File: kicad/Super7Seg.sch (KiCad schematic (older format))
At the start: 37 parts, among them CON1 AVR-ISP-6, IC1 ATMEGA328P-P, IC2 74HC238, P1 CONN_01X13, P2 CONN_01X09, P3 CONN_01X13, P4 CONN_01X09, P5 UART, P6 CONN_01X02, P7 CONN_01X02, U1 ULN2003A

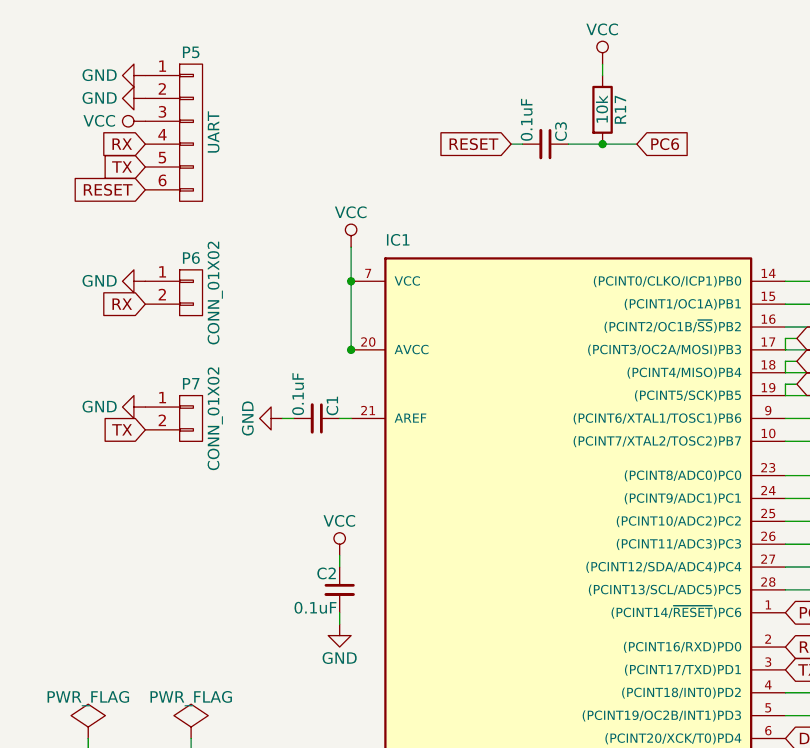
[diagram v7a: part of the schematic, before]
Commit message: Removed AREF cap.
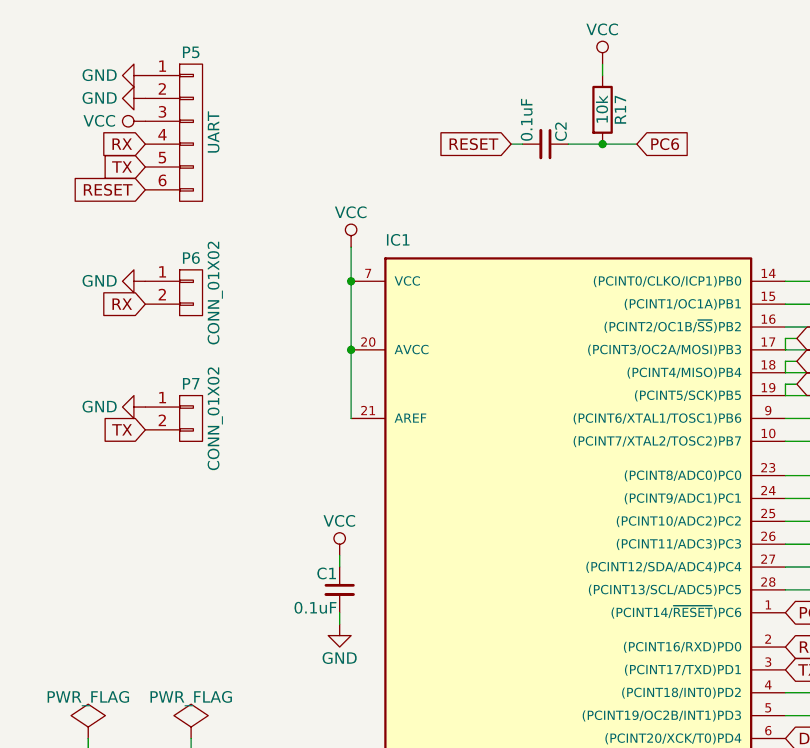
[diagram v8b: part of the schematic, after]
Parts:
- removed C1: 0.1uF, Capacitors_ThroughHole:C_Disc_D3_P2.5, symbol C_Small
- renumbered C2 to C1, C3 to C2
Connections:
- net VCC: now also IC1.21 (AREF)
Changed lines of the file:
@@
 Connection ~ 6750 2100
 Wire Wire Line
-	6750 1650 6750 2100
-$Comp
-L C_Small C2
+	6750 1650 6750 2400
+$Comp
+L C_Small C1
 U 1 1 585DF6FF
 P 6700 3150
-F 0 "C2" H 6710 3220 50  0000 L CNN
+F 0 "C1" H 6710 3220 50  0000 L CNN
 F 1 "0.1uF" H 6710 3070 50  0000 L CNN
 F 2 "Capacitors_ThroughHole:C_Disc_D3_P2.5" H 6700 3150 50  0001 C CNN
@@
 	-1   0    0    -1
 $EndComp
-$Comp
-L C_Small C1
-U 1 1 585E1667
-P 6600 2400
-F 0 "C1" H 6610 2470 50  0000 L CNN
-F 1 "0.1uF" H 6610 2320 50  0000 L CNN
-F 2 "Capacitors_ThroughHole:C_Disc_D3_P2.5" H 6600 2400 50  0001 C CNN
-F 3 "" H 6600 2400 50  0000 C CNN
-	1    6600 2400
-	0    1    -1   0
-$EndComp
-Wire Wire Line
-	6450 2400 6500 2400
-Wire Wire Line
-	6700 2400 6750 2400
 Text GLabel 8000 1200 2    50   Input ~ 0
 PC6
@@
 RESET
 $Comp
-L C_Small C3
+L C_Small C2
 U 1 1 585E2D7F
 P 7600 1200
-F 0 "C3" H 7610 1270 50  0000 L CNN
+F 0 "C2" H 7610 1270 50  0000 L CNN
 F 1 "0.1uF" H 7610 1120 50  0000 L CNN
 F 2 "Capacitors_ThroughHole:C_Disc_D3_P2.5" H 7600 1200 50  0001 C CNN
@@
 $EndComp
 $Comp
-L GND #PWR06
-U 1 1 585E166D
-P 6450 2400
-F 0 "#PWR06" H 6450 2150 50  0001 C CNN
-F 1 "GND" H 6450 2250 50  0000 C CNN
-F 2 "" H 6450 2400 50  0000 C CNN
-F 3 "" H 6450 2400 50  0000 C CNN
-	1    6450 2400
-	0    1    -1   0
-$EndComp
-$Comp
-L PWR_FLAG #FLG07
+L PWR_FLAG #FLG06
 U 1 1 585EE745
 P 5600 3800
-F 0 "#FLG07" H 5600 3895 50  0001 C CNN
+F 0 "#FLG06" H 5600 3895 50  0001 C CNN
 F 1 "PWR_FLAG" H 5600 3980 50  0000 C CNN
 F 2 "" H 5600 3800 50  0000 C CNN
@@
 $EndComp
 $Comp
-L GND #PWR08
+L GND #PWR07
 U 1 1 585EEC8B
 P 5600 3850
-F 0 "#PWR08" H 5600 3600 50  0001 C CNN
+F 0 "#PWR07" H 5600 3600 50  0001 C CNN
 F 1 "GND" H 5600 3700 50  0000 C CNN
 F 2 "" H 5600 3850 50  0000 C CNN
@@
 $EndComp
 $Comp
-L VCC #PWR09
+L VCC #PWR08
 U 1 1 585EED05
 P 6050 3850
-F 0 "#PWR09" H 6050 3700 50  0001 C CNN
+F 0 "#PWR08" H 6050 3700 50  0001 C CNN
 F 1 "VCC" H 6050 4000 50  0000 C CNN
 F 2 "" H 6050 3850 50  0000 C CNN
@@
 $EndComp
 $Comp
-L PWR_FLAG #FLG010
+L PWR_FLAG #FLG09
 U 1 1 585EED7F
 P 6050 3800
-F 0 "#FLG010" H 6050 3895 50  0001 C CNN
+F 0 "#FLG09" H 6050 3895 50  0001 C CNN
 F 1 "PWR_FLAG" H 6050 3980 50  0000 C CNN
 F 2 "" H 6050 3800 50  0000 C CNN
@@
 	6750 4100 6750 4000
 $Comp
-L VCC #PWR011
+L VCC #PWR010
 U 1 1 585F09FF
 P 5850 1100
-F 0 "#PWR011" H 5850 950 50  0001 C CNN
+F 0 "#PWR010" H 5850 950 50  0001 C CNN
 F 1 "VCC" V 5850 1300 50  0000 C CNN
 F 2 "" H 5850 1100 50  0000 C CNN
@@
 $EndComp
 $Comp
-L GND #PWR012
+L GND #PWR011
 U 1 1 585F0B43
 P 5850 900
-F 0 "#PWR012" H 5850 650 50  0001 C CNN
+F 0 "#PWR011" H 5850 650 50  0001 C CNN
 F 1 "GND" V 5850 700 50  0000 C CNN
 F 2 "" H 5850 900 50  0000 C CNN
@@
 $EndComp
 $Comp
-L GND #PWR013
+L GND #PWR012
 U 1 1 585F7588
 P 5850 1800
-F 0 "#PWR013" H 5850 1550 50  0001 C CNN
+F 0 "#PWR012" H 5850 1550 50  0001 C CNN
 F 1 "GND" V 5850 1600 50  0000 C CNN
 F 2 "" H 5850 1800 50  0000 C CNN
@@
 $EndComp
 $Comp
-L GND #PWR014
+L GND #PWR013
 U 1 1 585F7722
 P 5850 2350
-F 0 "#PWR014" H 5850 2100 50  0001 C CNN
+F 0 "#PWR013" H 5850 2100 50  0001 C CNN
 F 1 "GND" V 5850 2150 50  0000 C CNN
 F 2 "" H 5850 2350 50  0000 C CNN
@@
 TX
 $Comp
-L GND #PWR015
+L GND #PWR014
 U 1 1 585F7F59
 P 7400 4950
-F 0 "#PWR015" H 7400 4700 50  0001 C CNN
+F 0 "#PWR014" H 7400 4700 50  0001 C CNN
 F 1 "GND" V 7400 4750 50  0000 C CNN
 F 2 "" H 7400 4950 50  0000 C CNN
@@
 MISO
 $Comp
-L VCC #PWR016
+L VCC #PWR015
 U 1 1 585F951B
 P 7400 4750
-F 0 "#PWR016" H 7400 4600 50  0001 C CNN
+F 0 "#PWR015" H 7400 4600 50  0001 C CNN
 F 1 "VCC" H 7400 4900 50  0000 C CNN
 F 2 "" H 7400 4750 50  0000 C CNN
@@
 $EndComp
 $Comp
-L GND #PWR?
+L GND #PWR016
 U 1 1 586ACCF7
 P 10500 4300
-F 0 "#PWR?" H 10500 4050 50  0001 C CNN
+F 0 "#PWR016" H 10500 4050 50  0001 C CNN
 F 1 "GND" H 10500 4150 50  0000 C CNN
 F 2 "" H 10500 4300 50  0000 C CNN
@@
 	10550 4300 10550 4400
 $Comp
-L VCC #PWR?
+L VCC #PWR017
 U 1 1 586ADBCB
 P 10500 4500
-F 0 "#PWR?" H 10500 4350 50  0001 C CNN
+F 0 "#PWR017" H 10500 4350 50  0001 C CNN
 F 1 "VCC" H 10500 4650 50  0000 C CNN
 F 2 "" H 10500 4500 50  0000 C CNN
@@
 $EndComp
 $Comp
-L VCC #PWR?
+L VCC #PWR018
 U 1 1 586AE442
 P 10500 3500
-F 0 "#PWR?" H 10500 3350 50  0001 C CNN
+F 0 "#PWR018" H 10500 3350 50  0001 C CNN
 F 1 "VCC" H 10500 3650 50  0000 C CNN
 F 2 "" H 10500 3500 50  0000 C CNN
@@
 	10550 3500 10500 3500
 $Comp
-L GND #PWR?
+L GND #PWR019
 U 1 1 586AE701
 P 10500 3700
-F 0 "#PWR?" H 10500 3450 50  0001 C CNN
+F 0 "#PWR019" H 10500 3450 50  0001 C CNN
 F 1 "GND" H 10500 3550 50  0000 C CNN
 F 2 "" H 10500 3700 50  0000 C CNN
@@
 DC_C
 $Comp
-L GND #PWR?
+L GND #PWR020
 U 1 1 5871A688
 P 5850 1000
-F 0 "#PWR?" H 5850 750 50  0001 C CNN
+F 0 "#PWR020" H 5850 750 50  0001 C CNN
 F 1 "GND" V 5850 800 50  0000 C CNN
 F 2 "" H 5850 1000 50  0000 C CNN
